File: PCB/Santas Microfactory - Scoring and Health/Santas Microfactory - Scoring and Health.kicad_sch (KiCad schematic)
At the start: 0 parts

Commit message: Scoring and Health Board Layout Done
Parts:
- added D1, D10, D100, D101, D102, D103, D104, D105, D106, D107, D108, D109, D11, D110, D111, D112, D113, D114, D115, D116, D117, D118, D119, D12, D120, D121, D122, D123, D124, D125, D126, D127, D128, D129, D13, D130, D131, D132, D133, D134, D135, D136, D137, D138, D139, D14, D140, D141, D142, D143, D144, D145, D146, D147, D148, D149, D15, D150, D151, D152, D153, D154, D155, D156, D157, D158, D159, D16, D160, D161, D162, D163, D164, D165, D166, D167, D168, D169, D17, D170, D171, D172, D173, D174, D175, D176, D177, D178, D179, D18, D180, D181, D182, D183, D184, D185, D186, D187, D188, D189, D19, D190, D191, D192, D193, D194, D195, D196, D197, D198, D199, D2, D20, D200, D201, D202, D203, D204, D205, D206, D207, D208, D209, D21, D210, D211, D212, D213, D214, D215, D216, D217, D218, D219, D22, D220, D221, D222, D223, D224, D225, D226, D227, D228, D229, D23, D230, D231, D232, D233, D234, D235, D236, D237, D238, D239, D24, D240, D241, D242, D243, D244, D245, D246, D247, D248, D249, D25, D250, D251, D252, D253, D254, D255, D256, D257, D258, D259, D26, D260, D261, D262, D263, D264, D265, D266, D267, D268, D269, D27, D270, D271, D272, D273, D274, D275, D276, D277, D278, D279, D28, D280, D281, D282, D283, D284, D285, D286, D287, D288, D289, D29, D290, D291, D292, D293, D294, D295, D296, D297, D298, D299, D3, D30, D300, D301, D302, D303, D304, D305, D306, D307, D308, D309, D31, D310, D311, D312, D313, D32, D33, D34, D35, D36, D37, D38, D39, D4, D40, D41, D42, D43, D44, D45, D46, D47, D48, D49, D5, D50, D51, D52, D53, D54, D55, D56, D57, D58, D59, D6, D60, D61, D62, D63, D64, D65, D66, D67, D68, D69, D7, D70, D71, D72, D73, D74, D75, D76, D77, D78, D79, D8, D80, D81, D82, D83, D84, D85, D86, D87, D88, D89, D9, D90, D91, D92, D93, D94, D95, D96, D97, D98, D99: D, Diode_THT:D_DO-35_SOD27_P2.54mm_Vertical_AnodeUp, symbol Device:D
- added J2: Conn_01x08_Pin, Connector_PinHeader_2.54mm:PinHeader_1x08_P2.54mm_Horizontal, symbol Connector:Conn_01x08_Pin
- added J3: Conn_01x04_Pin, Connector_PinHeader_2.54mm:PinHeader_1x04_P2.54mm_Horizontal, symbol Connector:Conn_01x04_Pin
- added J4: Bus_PCI_Express_x16, Connector_PCBEdge:BUS_PCIexpress_x16, symbol Connector:Bus_PCI_Express_x16
- added Q1, Q10, Q11, Q12, Q13, Q14, Q15, Q16, Q17, Q18, Q19, Q2, Q20, Q21, Q22, Q23, Q24, Q25, Q26, Q27, Q28, Q29, Q3, Q30, Q31, Q32, Q33, Q34, Q35, Q36, Q37, Q38, Q39, Q4, Q40, Q41, Q42, Q43, Q44, Q45, Q46, Q47, Q48, Q49, Q5, Q50, Q51, Q52, Q53, Q54, Q55, Q56, Q57, Q58, Q59, Q6, Q60, Q61, Q62, Q63, Q64, Q65, Q66, Q67, Q68, Q69, Q7, Q70, Q71, Q72, Q73, Q74, Q75, Q76, Q77, Q78, Q79, Q8, Q80, Q81, Q9: NPN, Package_TO_SOT_THT:TO-92L_Inline, symbol Simulation_SPICE:NPN
- added R1, R10, R100, R101, R102, R103, R104, R105, R106, R107, R108, R109, R11, R110, R111, R112, R113, R114, R115, R116, R117, R118, R119, R12, R120, R121, R122, R123, R124, R125, R126, R127, R128, R129, R13, R130, R131, R132, R133, R134, R135, R136, R137, R138, R139, R14, R140, R141, R142, R143, R144, R145, R146, R147, R148, R149, R15, R150, R151, R152, R153, R154, R155, R156, R157, R158, R159, R16, R160, R161, R162, R163, R164, R165, R166, R167, R168, R169, R17, R170, R171, R172, R173, R174, R175, R176, R177, R178, R179, R18, R180, R181, R182, R183, R184, R185, R186, R187, R188, R189, R19, R190, R191, R192, R193, R194, R195, R196, R197, R198, R199, R2, R20, R200, R201, R202, R203, R204, R205, R206, R207, R208, R209, R21, R210, R211, R212, R213, R214, R215, R216, R217, R218, R219, R22, R220, R221, R222, R223, R224, R225, R226, R227, R228, R229, R23, R230, R231, R232, R233, R24, R25, R26, R27, R28, R29, R3, R30, R31, R32, R33, R34, R35, R36, R37, R38, R39, R4, R40, R41, R42, R43, R44, R45, R46, R47, R48, R49, R5, R50, R51, R52, R53, R54, R55, R56, R57, R58, R59, R6, R60, R61, R62, R63, R64, R65, R66, R67, R68, R69, R7, R70, R71, R72, R73, R74, R75, R76, R77, R78, R79, R8, R80, R81, R82, R83, R84, R85, R86, R87, R88, R89, R9, R90, R91, R92, R93, R94, R95, R96, R97, R98, R99: 10k, Resistor_THT:R_Axial_DIN0207_L6.3mm_D2.5mm_P2.54mm_Vertical, symbol Device:R
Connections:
- new net: D13.2 (A), D14.1 (K), D30.2 (A), R20.2
- new net: D14.2 (A), D31.2 (A), Q2.2 (B), R21.2
- new net: D155.1 (K), Q46.1 (C), R150.2
- new net: D155.2 (A), D180.2 (A), D207.2 (A), R118.2
- new net: D110.2 (A), D94.2 (A), Q24.2 (B), R81.2
- new net: D4.2 (A), D50.1 (K), D9.2 (A), Q11.2 (B), R8.2
- new net: D19.2 (A), D20.1 (K), D36.2 (A), R26.2
- new net: D20.2 (A), D37.2 (A), Q5.2 (B), R27.2
- new net: D122.2 (A), D138.2 (A), D146.1 (K), R101.2
- new net: D274.1 (K), Q75.1 (C), R226.2
- new net: D231.2 (A), D232.1 (K), D244.2 (A), R184.2
- new net: D276.2 (A), D286.2 (A), D287.2 (A), R207.2
- new net: D33.1 (K), D49.1 (K), Q15.1 (C), R36.2
- new net: D56.2 (A), D73.2 (A), Q15.2 (B), R52.2
- new net: D19.1 (K), Q11.1 (C), R16.2
- new net: D47.2 (A), D64.2 (A), D72.1 (K), R43.2
- new net: D158.2 (A), D184.2 (A), D185.2 (A), R121.2
- new net: D100.1 (K), D115.2 (A), D99.2 (A), R86.2
- new net: D17.2 (A), D18.1 (K), D34.2 (A), R24.2
- new net: D18.2 (A), D35.2 (A), Q4.2 (B), R25.2
- new net: D294.2 (A), D303.2 (A), Q72.2 (B), R218.2
- new net: D248.2 (A), D261.2 (A), D267.1 (K), R192.2
- new net: D254.2 (A), D267.2 (A), Q66.2 (B), R198.2
- new net: D108.1 (K), D122.1 (K), Q35.1 (C), R92.2
- new net: D252.2 (A), D265.2 (A), D271.1 (K), R196.2
- new net: D258.2 (A), D271.2 (A), Q70.2 (B), R202.2
- new net: D153.2 (A), D177.2 (A), D206.2 (A), R116.2
- new net: D259.2 (A), D272.2 (A), Q71.2 (B), R203.2
- new net: D51.2 (A), D68.2 (A), D76.1 (K), R47.2
- new net: D235.1 (K), D249.1 (K), Q66.1 (C), R186.2
- new net: D11.1 (K), Q9.1 (C), R14.2
- new net: D11.2 (A), D12.1 (K), D28.2 (A), R18.2
- new net: D17.1 (K), D56.1 (K), Q3.1 (C), R6.2
- new net: D16.2 (A), D33.2 (A), Q3.2 (B), R23.2
- new net: D15.2 (A), D16.1 (K), D32.2 (A), R22.2
- new net: D161.1 (K), Q52.1 (C), R156.2
- new net: D161.2 (A), D189.2 (A), D210.2 (A), R124.2
- new net: D107.2 (A), D91.2 (A), D92.1 (K), R78.2
- new net: D163.2 (A), D192.2 (A), D211.2 (A), R126.2
- new net: D251.2 (A), D264.2 (A), D270.1 (K), R195.2
- new net: D131.1 (K), D97.1 (K), Q25.1 (C), R65.2
- new net: D119.1 (K), D79.2 (A), D83.2 (A), Q29.2 (B), R58.2
- new net: D87.1 (K), Q29.1 (C), R70.2
- new net: D116.1 (K), D126.1 (K), Q39.1 (C), R96.2
- new net: D55.2 (A), D72.2 (A), Q14.2 (B), R51.2
- new net: D250.2 (A), D263.2 (A), D269.1 (K), R194.2
- new net: D157.1 (K), Q48.1 (C), R152.2
- new net: D123.2 (A), D139.2 (A), D147.1 (K), R102.2
- new net: D131.2 (A), D147.2 (A), Q37.2 (B), R110.2
- new net: D41.1 (K), D53.1 (K), Q19.1 (C), R40.2
- new net: D24.2 (A), D41.2 (A), Q7.2 (B), R31.2
- new net: D273.2 (A), D282.2 (A), D299.2 (A), R204.2
- new net: D121.1 (K), D80.2 (A), D84.2 (A), Q30.2 (B), R61.2
- new net: D13.1 (K), D54.1 (K), Q1.1 (C), R3.2
- new net: D12.2 (A), D29.2 (A), Q1.2 (B), R19.2
- new net: D22.2 (A), D39.2 (A), Q6.2 (B), R29.2
- new net: D91.1 (K), Q30.1 (C), R71.2
- new net: D130.2 (A), D146.2 (A), Q36.2 (B), R109.2
- new net: D109.2 (A), D93.2 (A), D94.1 (K), R80.2
- new net: D158.1 (K), Q47.1 (C), R151.2
- new net: D120.2 (A), D136.2 (A), D144.1 (K), R99.2
- new net: D123.1 (K), D81.2 (A), D85.2 (A), Q31.2 (B), R64.2
- new net: D133.2 (A), D149.2 (A), Q39.2 (B), R112.2
- new net: D224.2 (A), D237.2 (A), Q58.2 (B), R177.2
- new net: D119.2 (A), D135.2 (A), D143.1 (K), R98.2
- new net: D215.2 (A), D219.2 (A), D250.1 (K), Q64.2 (B), R165.2
- new net: D273.1 (K), Q76.1 (C), R227.2
- new net: D112.1 (K), D124.1 (K), Q37.1 (C), R94.2
- new net: D112.2 (A), D96.2 (A), Q25.2 (B), R83.2
- new net: D23.1 (K), Q12.1 (C), R17.2
- new net: D46.2 (A), D63.2 (A), D71.1 (K), R42.2
- new net: D151.1 (K), Q42.1 (C), R146.2
- new net: D154.2 (A), D178.2 (A), D179.2 (A), R117.2
- new net: D166.1 (K), Q55.1 (C), R159.2
- new net: D152.1 (K), Q41.1 (C), R145.2
- new net: D214.2 (A), D218.2 (A), D248.1 (K), Q63.2 (B), R162.2
- new net: D125.1 (K), D82.2 (A), D86.2 (A), Q32.2 (B), R67.2
- new net: D229.1 (K), Q65.1 (C), R173.2
- new net: D216.2 (A), D220.2 (A), D252.1 (K), Q65.2 (B), R168.2
- new net: D154.1 (K), Q43.1 (C), R147.2
- new net: D275.1 (K), Q78.1 (C), R229.2
- new net: D221.1 (K), Q63.1 (C), R171.2
- new net: D100.2 (A), D116.2 (A), Q27.2 (B), R87.2
- new net: D160.2 (A), D187.2 (A), D188.2 (A), R123.2
- new net: D53.2 (A), D70.2 (A), D78.1 (K), R49.2
- new net: D152.2 (A), D175.2 (A), D176.2 (A), R115.2
- new net: D278.1 (K), Q79.1 (C), R230.2
- new net: D10.2 (A), D5.2 (A), D52.1 (K), Q12.2 (B), R11.2
- new net: D23.2 (A), D24.1 (K), D40.2 (A), R30.2
- new net: D127.1 (K), D89.1 (K), Q21.1 (C), R59.2
- new net: D25.2 (A), D26.1 (K), D42.2 (A), R32.2
- new net: D101.1 (K), D133.1 (K), Q27.1 (C), R68.2
- new net: D101.2 (A), D102.1 (K), D117.2 (A), R88.2
- new net: D153.1 (K), Q44.1 (C), R148.2
- new net: D61.2 (A), D78.2 (A), Q20.2 (B), R57.2
- new net: D164.2 (A), D193.2 (A), D194.2 (A), R127.2
- new net: D312.2 (A), D313.2 (A), Q81.2 (B), R233.2
- new net: D121.2 (A), D137.2 (A), D145.1 (K), R100.2
- new net: D157.2 (A), D183.2 (A), D208.2 (A), R120.2
- new net: D151.2 (A), D174.2 (A), D205.2 (A), R114.2
- new net: D274.2 (A), D283.2 (A), D284.2 (A), R205.2
- new net: D166.2 (A), D196.2 (A), D197.2 (A), R129.2
- new net: D165.2 (A), D195.2 (A), D212.2 (A), R128.2
- new net: D253.2 (A), D266.2 (A), D272.1 (K), R197.2
- new net: D50.2 (A), D67.2 (A), D75.1 (K), R46.2
- new net: D37.1 (K), D51.1 (K), Q17.1 (C), R38.2
- new net: D113.2 (A), D97.2 (A), D98.1 (K), R84.2
- new net: D25.1 (K), D60.1 (K), Q7.1 (C), R12.2
- new net: D15.1 (K), Q10.1 (C), R15.2
- new net: D223.1 (K), D254.1 (K), Q57.1 (C), R163.2
- new net: D222.2 (A), D235.2 (A), Q57.2 (B), R175.2
- new net: D125.2 (A), D141.2 (A), D149.1 (K), R104.2
- new net: D2.2 (A), D46.1 (K), D7.2 (A), Q9.2 (B), R2.2
- new net: D243.1 (K), D253.1 (K), Q70.1 (C), R190.2
- new net: D127.2 (A), D143.2 (A), Q33.2 (B), R106.2
- new net: D29.1 (K), D47.1 (K), Q13.1 (C), R34.2
- new net: D54.2 (A), D71.2 (A), Q13.2 (B), R50.2
- new net: D26.2 (A), D43.2 (A), Q8.2 (B), R33.2
- new net: D304.1 (K), Q74.1 (C), R219.2
- new net: D232.2 (A), D245.2 (A), Q62.2 (B), R185.2
- new net: D278.2 (A), D289.2 (A), D290.2 (A), R209.2
- new net: D225.2 (A), D226.1 (K), D238.2 (A), R178.2
- new net: D226.2 (A), D239.2 (A), Q59.2 (B), R179.2
- new net: D57.2 (A), D74.2 (A), Q16.2 (B), R53.2
- new net: D111.2 (A), D95.2 (A), D96.1 (K), R82.2
- new net: D49.2 (A), D66.2 (A), D74.1 (K), R45.2
- new net: D229.2 (A), D230.1 (K), D242.2 (A), R182.2
- new net: D48.2 (A), D65.2 (A), D73.1 (K), R44.2
- new net: D102.2 (A), D118.2 (A), Q28.2 (B), R89.2
- new net: D221.2 (A), D222.1 (K), D234.2 (A), R174.2
- new net: D164.1 (K), Q53.1 (C), R157.2
- new net: D126.2 (A), D142.2 (A), D150.1 (K), R105.2
- new net: D134.2 (A), D150.2 (A), Q40.2 (B), R113.2
- new net: D162.2 (A), D190.2 (A), D191.2 (A), R125.2
- new net: D160.1 (K), Q49.1 (C), R153.2
- new net: D277.1 (K), Q80.1 (C), R231.2
- new net: D162.1 (K), Q51.1 (C), R155.2
- new net: D281.2 (A), D293.2 (A), D307.1 (K), R214.2
- new net: D277.2 (A), D288.2 (A), D301.2 (A), R208.2
- new net: D257.2 (A), D270.2 (A), Q69.2 (B), R201.2
- new net: D227.2 (A), D228.1 (K), D240.2 (A), R180.2
- new net: D114.2 (A), D98.2 (A), Q26.2 (B), R85.2
- new net: D59.2 (A), D76.2 (A), Q18.2 (B), R55.2
- new net: D163.1 (K), Q54.1 (C), R158.2
- new net: D106.2 (A), D90.2 (A), Q22.2 (B), R77.2
- new net: D129.1 (K), D93.1 (K), Q23.1 (C), R62.2
- new net: D228.2 (A), D241.2 (A), Q60.2 (B), R181.2
- new net: D276.1 (K), Q77.1 (C), R228.2
- new net: D256.2 (A), D269.2 (A), Q68.2 (B), R200.2
- new net: D129.2 (A), D145.2 (A), Q35.2 (B), R108.2
- new net: D132.2 (A), D148.2 (A), Q38.2 (B), R111.2
- new net: D159.1 (K), Q50.1 (C), R154.2
- new net: D227.1 (K), D256.1 (K), Q59.1 (C), R166.2
- new net: D124.2 (A), D140.2 (A), D148.1 (K), R103.2
- new net: D223.2 (A), D224.1 (K), D236.2 (A), R176.2
- new net: D103.2 (A), D87.2 (A), D88.1 (K), R74.2
- new net: D255.2 (A), D268.2 (A), Q67.2 (B), R199.2
- new net: D298.1 (K), D308.1 (K), Q73.2 (B), R223.1
- new net: D104.1 (K), D120.1 (K), Q33.1 (C), R90.2
- new net: D3.2 (A), D48.1 (K), D8.2 (A), Q10.2 (B), R5.2
- new net: D156.2 (A), D181.2 (A), D182.2 (A), R119.2
- new net: D99.1 (K), Q32.1 (C), R73.2
- new net: D105.2 (A), D89.2 (A), D90.1 (K), R76.2
- new net: D156.1 (K), Q45.1 (C), R149.2
- new net: D58.2 (A), D75.2 (A), Q17.2 (B), R54.2
- new net: D231.1 (K), D258.1 (K), Q61.1 (C), R169.2
- new net: D21.1 (K), D58.1 (K), Q5.1 (C), R9.2
- new net: D230.2 (A), D243.2 (A), Q61.2 (B), R183.2
- new net: D302.2 (A), D309.2 (A), Q74.2 (B), R224.2
- new net: D159.2 (A), D186.2 (A), D209.2 (A), R122.2
- new net: D225.1 (K), Q64.1 (C), R172.2
- new net: D60.2 (A), D77.2 (A), Q19.2 (B), R56.2
- new net: D275.2 (A), D285.2 (A), D300.2 (A), R206.2
- new net: D52.2 (A), D69.2 (A), D77.1 (K), R48.2
- new net: D95.1 (K), Q31.1 (C), R72.2
- new net: D128.2 (A), D144.2 (A), Q34.2 (B), R107.2
- new net: D108.2 (A), D92.2 (A), Q23.2 (B), R79.2
- new net: D21.2 (A), D22.1 (K), D38.2 (A), R28.2
- new net: D249.2 (A), D262.2 (A), D268.1 (K), R193.2
- new net: D165.1 (K), Q56.1 (C), R160.2
- new net: D239.1 (K), D251.1 (K), Q68.1 (C), R188.2
- new net: D293.1 (K), Q73.1 (C), R213.2
- new net: D104.2 (A), D88.2 (A), Q21.2 (B), R75.2
- new net +5V: J4.A10 (+3.3V), J4.A2 (+12V), J4.A3 (+12V), J4.A9 (+3.3V), J4.B1 (+12V), J4.B10 (3.3Vaux), J4.B2 (+12V), J4.B3 (+12V), J4.B8 (+3.3V), R10.1, R100.1, R101.1, R102.1, R103.1, R104.1, R105.1, R106.1, R107.1, R108.1, R109.1, R11.1, R110.1, R111.1, R112.1, R113.1, R114.1, R115.1, R116.1, R117.1, R118.1, R119.1, R12.1, R120.1, R121.1, R122.1, R123.1, R124.1, R125.1, R126.1, R127.1, R128.1, R129.1, R13.1, R130.1, R131.1, R132.1, R133.1, R134.1, R135.1, R136.1, R14.1, R145.1, R146.1, R147.1, R148.1, R149.1, R15.1, R150.1, R151.1, R152.1, R153.1, R154.1, R155.1, R156.1, R157.1, R158.1, R159.1, R16.1, R160.1, R162.1, R163.1, R164.1, R165.1, R166.1, R167.1, R168.1, R169.1, R17.1, R170.1, R171.1, R172.1, R173.1, R174.1, R175.1, R176.1, R177.1, R178.1, R179.1, R18.1, R180.1, R181.1, R182.1, R183.1, R184.1, R185.1, R186.1, R187.1, R188.1, R189.1, R19.1, R190.1, R191.1, R192.1, R193.1, R194.1, R195.1, R196.1, R197.1, R198.1, R199.1, R2.1, R20.1, R200.1, R201.1, R202.1, R203.1, R204.1, R205.1, R206.1, R207.1, R208.1, R209.1, R21.1, R210.1, R211.1, R212.1, R213.1, R214.1, R218.1, R219.1, R22.1, R220.1, R221.1, R222.1, R224.1, R225.1, R226.1, R227.1, R228.1, R229.1, R23.1, R230.1, R231.1, R232.1, R233.1, R24.1, R25.1, R26.1, R27.1, R28.1, R29.1, R3.1, R30.1, R31.1, R32.1, R33.1, R34.1, R35.1, R36.1, R37.1, R38.1, R39.1, R4.1, R40.1, R41.1, R42.1, R43.1, R44.1, R45.1, R46.1, R47.1, R48.1, R49.1, R5.1, R50.1, R51.1, R52.1, R53.1, R54.1, R55.1, R56.1, R57.1, R58.1, R59.1, R6.1, R60.1, R61.1, R62.1, R63.1, R64.1, R65.1, R66.1, R67.1, R68.1, R69.1, R7.1, R70.1, R71.1, R72.1, R73.1, R74.1, R75.1, R76.1, R77.1, R78.1, R79.1, R8.1, R80.1, R81.1, R82.1, R83.1, R84.1, R85.1, R86.1, R87.1, R88.1, R89.1, R9.1, R90.1, R91.1, R92.1, R93.1, R94.1, R95.1, R96.1, R97.1, R98.1, R99.1
- new net CLK: D103.1 (K), D107.1 (K), D111.1 (K), D115.1 (K), D135.1 (K), D137.1 (K), D139.1 (K), D141.1 (K), D234.1 (K), D238.1 (K), D242.1 (K), D261.1 (K), D263.1 (K), D265.1 (K), D28.1 (K), D32.1 (K), D36.1 (K), D40.1 (K), D63.1 (K), D65.1 (K), D67.1 (K), D69.1 (K), J4.A13 (REFCLK+)
- new net CLK_TICK: J4.A1 (~{PRSNT1})
- new net CORR_0: D1.2 (A), J4.B82 (RSVD)
- new net CORR_1: D6.2 (A), J4.A50 (RSVD)
- new net CORR_2: D27.2 (A), J4.A33 (RSVD)
- new net CORR_3: D44.2 (A), J4.B30 (RSVD)
- new net CORR_4: D45.2 (A), J4.A32 (RSVD)
- new net CORR_5: D62.2 (A), J4.A19 (RSVD)
- new net DAMAGE: D213.1 (K), D217.1 (K), D233.1 (K), D246.1 (K), D247.1 (K), D260.1 (K), D279.1 (K), D282.1 (K), Q75.2 (B), R161.1
- new net DEATH: D294.1 (K), D307.2 (A), D311.2 (A), R225.2
- new net DSTEP1: D279.2 (A), D280.1 (K), D285.1 (K), D291.2 (A), Q77.2 (B), R211.2
- new net DSTEP2: D280.2 (A), D288.1 (K), D292.2 (A), Q79.2 (B), R212.2
- new net GND: J4.A12 (GND), J4.A15 (GND), J4.A18 (GND), J4.A20 (GND), J4.A23 (GND), J4.A24 (GND), J4.A27 (GND), J4.A28 (GND), J4.A31 (GND), J4.A34 (GND), J4.A37 (GND), J4.A38 (GND), J4.A4 (GND), J4.A41 (GND), J4.A42 (GND), J4.A45 (GND), J4.A46 (GND), J4.A49 (GND), J4.A51 (GND), J4.A54 (GND), J4.A55 (GND), J4.A58 (GND), J4.A59 (GND), J4.A62 (GND), J4.A63 (GND), J4.A66 (GND), J4.A67 (GND), J4.A70 (GND), J4.A71 (GND), J4.A74 (GND), J4.A75 (GND), J4.A78 (GND), J4.A79 (GND), J4.A82 (GND), J4.B13 (GND), J4.B16 (GND), J4.B18 (GND), J4.B21 (GND), J4.B22 (GND), J4.B25 (GND), J4.B26 (GND), J4.B29 (GND), J4.B32 (GND), J4.B35 (GND), J4.B36 (GND), J4.B39 (GND), J4.B4 (GND), J4.B40 (GND), J4.B43 (GND), J4.B44 (GND), J4.B47 (GND), J4.B49 (GND), J4.B52 (GND), J4.B53 (GND), J4.B56 (GND), J4.B57 (GND), J4.B60 (GND), J4.B61 (GND), J4.B64 (GND), J4.B65 (GND), J4.B68 (GND), J4.B69 (GND), J4.B7 (GND), J4.B72 (GND), J4.B73 (GND), J4.B76 (GND), J4.B77 (GND), J4.B80 (GND), Q1.3 (E), Q10.3 (E), Q11.3 (E), Q12.3 (E), Q13.3 (E), Q14.3 (E), Q15.3 (E), Q16.3 (E), Q17.3 (E), Q18.3 (E), Q19.3 (E), Q2.3 (E), Q20.3 (E), Q21.3 (E), Q22.3 (E), Q23.3 (E), Q24.3 (E), Q25.3 (E), Q26.3 (E), Q27.3 (E), Q28.3 (E), Q29.3 (E), Q3.3 (E), Q30.3 (E), Q31.3 (E), Q32.3 (E), Q33.3 (E), Q34.3 (E), Q35.3 (E), Q36.3 (E), Q37.3 (E), Q38.3 (E), Q39.3 (E), Q4.3 (E), Q40.3 (E), Q41.3 (E), Q42.3 (E), Q43.3 (E), Q44.3 (E), Q45.3 (E), Q46.3 (E), Q47.3 (E), Q48.3 (E), Q49.3 (E), Q5.3 (E), Q50.3 (E), Q51.3 (E), Q52.3 (E), Q53.3 (E), Q54.3 (E), Q55.3 (E), Q56.3 (E), Q57.3 (E), Q58.3 (E), Q59.3 (E), Q6.3 (E), Q60.3 (E), Q61.3 (E), Q62.3 (E), Q63.3 (E), Q64.3 (E), Q65.3 (E), Q66.3 (E), Q67.3 (E), Q68.3 (E), Q69.3 (E), Q7.3 (E), Q70.3 (E), Q71.3 (E), Q72.3 (E), Q73.3 (E), Q74.3 (E), Q75.3 (E), Q76.3 (E), Q77.3 (E), Q78.3 (E), Q79.3 (E), Q8.3 (E), Q80.3 (E), Q81.3 (E), Q9.3 (E), R1.2, R137.2, R138.2, R139.2, R140.2, R141.2, R142.2, R143.2, R144.2, R161.2, R215.2, R216.2, R217.2, R223.2
- new net HALT: D312.1 (K), J4.B48 (~{PRSNT2}), Q72.1 (C), R210.2
- new net HEART0: D245.1 (K), D295.1 (K), D305.1 (K), D310.1 (K), J3.1 (Pin_1), Q71.1 (C), R191.2
- new net HEART1: D295.2 (A), D304.2 (A), J3.2 (Pin_2), R220.2
- new net HEART2: D296.2 (A), D305.2 (A), J3.3 (Pin_3), R221.2
- new net HEART3: D297.2 (A), D306.2 (A), D310.2 (A), J3.4 (Pin_4), R222.2
- new net INPUT0: J4.B62 (PETp11)
- new net INPUT1: J4.B63 (PETn11)
- new net INPUT2: J4.B66 (PETp12)
- new net INPUT3: J4.B67 (PETn12)
- new net INPUT4: J4.B70 (PETp13)
- new net INPUT5: J4.B71 (PETn13)
- new net IN_C0: J4.B6 (SMDAT)
- new net IN_D0: D218.1 (K), D284.1 (K), D299.1 (K), R215.1
- new net IN_D1: D219.1 (K), D287.1 (K), D300.1 (K), R216.1
- new net IN_D2: D220.1 (K), D290.1 (K), D301.1 (K), R217.1
- new net IN_G0: J4.B5 (SMCLK)
- new net IN_H0: D176.1 (K), D205.1 (K), D7.1 (K), R137.1
- new net IN_H1: D179.1 (K), D206.1 (K), D8.1 (K), R138.1
- new net IN_H2: D182.1 (K), D207.1 (K), D9.1 (K), R139.1
- new net IN_H3: D10.1 (K), D185.1 (K), D208.1 (K), R140.1
- new net IN_H4: D188.1 (K), D209.1 (K), D83.1 (K), R141.1
- new net IN_H5: D191.1 (K), D210.1 (K), D84.1 (K), R142.1
- new net IN_H6: D194.1 (K), D211.1 (K), D85.1 (K), R143.1
- new net IN_H7: D197.1 (K), D212.1 (K), D86.1 (K), R144.1
- new net LOAD0: J4.B50 (PETp8)
- new net LOAD1: J4.B51 (PETn8)
- new net LOAD2: J4.B54 (PETp9)
- new net LOAD3: J4.B55 (PETn9)
- new net LOAD4: J4.B58 (PETp10)
- new net LOAD5: J4.B59 (PETn10)
- new net NCLK: D105.1 (K), D109.1 (K), D113.1 (K), D117.1 (K), D136.1 (K), D138.1 (K), D140.1 (K), D142.1 (K), D236.1 (K), D240.1 (K), D244.1 (K), D262.1 (K), D264.1 (K), D266.1 (K), D30.1 (K), D311.1 (K), D34.1 (K), D38.1 (K), D42.1 (K), D64.1 (K), D66.1 (K), D68.1 (K), D70.1 (K), J4.A14 (REFCLK-)
- new net NHALT: D303.1 (K), J4.B81 (~{PRSNT2}), Q81.1 (C), R232.2
- new net NOUT_D0: D237.1 (K), D297.1 (K), Q67.1 (C), R187.2
- new net NOUT_D1: D241.1 (K), D296.1 (K), D306.1 (K), Q69.1 (C), R189.2
- new net NOUT_H0: D31.1 (K), Q14.1 (C), R35.2
- new net NOUT_H1: D35.1 (K), Q16.1 (C), R37.2
- new net NOUT_H2: D39.1 (K), Q18.1 (C), R39.2
- new net NOUT_H3: D43.1 (K), Q20.1 (C), R41.2
- new net NOUT_H4: D106.1 (K), Q34.1 (C), R91.2
- new net NOUT_H5: D110.1 (K), Q36.1 (C), R93.2
- new net NOUT_H6: D114.1 (K), Q38.1 (C), R95.2
- new net NOUT_H7: D118.1 (K), Q40.1 (C), R97.2
- new net NRESET: D2.1 (K), D214.1 (K), D215.1 (K), D216.1 (K), D3.1 (K), D4.1 (K), D5.1 (K), D79.1 (K), D80.1 (K), D81.1 (K), D82.1 (K), J4.B31 (~{PRSNT2})
- new net OUT_D0: D255.1 (K), D283.1 (K), D291.1 (K), D298.2 (A), D302.1 (K), Q58.1 (C), Q76.2 (B), R164.2
- new net OUT_D1: D257.1 (K), D286.1 (K), D292.1 (K), D308.2 (A), D309.1 (K), Q60.1 (C), Q78.2 (B), R167.2
- new net OUT_D2: D259.1 (K), D281.1 (K), D289.1 (K), Q62.1 (C), Q80.2 (B), R170.2
- new net OUT_H0: D175.1 (K), D198.1 (K), D55.1 (K), J2.8 (Pin_8), Q2.1 (C), Q42.2 (B), R4.2
- new net OUT_H1: D178.1 (K), D199.1 (K), D57.1 (K), J2.7 (Pin_7), Q4.1 (C), Q44.2 (B), R7.2
- new net OUT_H2: D181.1 (K), D200.1 (K), D59.1 (K), J2.6 (Pin_6), Q46.2 (B), Q6.1 (C), R10.2
- new net OUT_H3: D184.1 (K), D201.1 (K), D61.1 (K), J2.5 (Pin_5), Q48.2 (B), Q8.1 (C), R13.2
- new net OUT_H4: D128.1 (K), D187.1 (K), D202.1 (K), J2.4 (Pin_4), Q22.1 (C), Q50.2 (B), R60.2
- new net OUT_H5: D130.1 (K), D190.1 (K), D203.1 (K), J2.3 (Pin_3), Q24.1 (C), Q52.2 (B), R63.2
- new net OUT_H6: D132.1 (K), D193.1 (K), D204.1 (K), J2.2 (Pin_2), Q26.1 (C), Q54.2 (B), R66.2
- new net OUT_H7: D134.1 (K), D196.1 (K), J2.1 (Pin_1), Q28.1 (C), Q56.2 (B), R69.2
- new net RESET: D313.1 (K), J4.B17 (~{PRSNT2})
- new net SEED_1: J4.B14 (PETp0)
- new net SEED_2: J4.B15 (PETn0)
- new net SEED_3: J4.B19 (PETp1)
- new net SEED_4: J4.B20 (PETn1)
- new net STEP0: D1.1 (K), D167.1 (K), D174.1 (K), D27.1 (K), D44.1 (K), D45.1 (K), D6.1 (K), D62.1 (K), Q41.2 (B), R1.1
- new net STEP1: D167.2 (A), D168.1 (K), D177.1 (K), D198.2 (A), Q43.2 (B), R130.2
- new net STEP2: D168.2 (A), D169.1 (K), D180.1 (K), D199.2 (A), Q45.2 (B), R131.2
- new net STEP3: D169.2 (A), D170.1 (K), D183.1 (K), D200.2 (A), Q47.2 (B), R132.2
- new net STEP4: D170.2 (A), D171.1 (K), D186.1 (K), D201.2 (A), Q49.2 (B), R133.2
- new net STEP5: D171.2 (A), D172.1 (K), D189.1 (K), D202.2 (A), Q51.2 (B), R134.2
- new net STEP6: D172.2 (A), D173.1 (K), D192.1 (K), D203.2 (A), Q53.2 (B), R135.2
- new net STEP7: D173.2 (A), D195.1 (K), D204.2 (A), Q55.2 (B), R136.2
- new net TAP_C2: J4.B24 (PETn2)
- new net TAP_C3: J4.B28 (PETn3)
- new net TAP_C5: J4.B34 (PETn4)
- new net TAP_C6: J4.B38 (PETn5)
- new net TAP_C8: J4.B42 (PETn6)
- new net TAP_C9: J4.B46 (PETn7)
- new net TAP_G2: J4.B23 (PETp2)
- new net TAP_G3: J4.B27 (PETp3)
- new net TAP_G5: J4.B33 (PETp4)
- new net TAP_G6: J4.B37 (PETp5)
- new net TAP_G8: J4.B41 (PETp6)
- new net TAP_G9: J4.B45 (PETp7)
- new net WRONG_0: D213.2 (A), J4.B12 (RSVD)
- new net WRONG_1: D217.2 (A), J4.B11 (~{WAKE})
- new net WRONG_2: D233.2 (A), J4.A11 (~{PERST})
- new net WRONG_3: D246.2 (A), J4.B9 (JTAG1)
- new net WRONG_4: D247.2 (A), J4.A5 (JTAG2)
- new net WRONG_5: D260.2 (A), J4.A6 (JTAG3)
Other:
- note added: "AND"
- note added: "D Flip-Flop"
- note added: "NAND"
- note added: "NOT"
- note added: "OR"
- note added: "RESETMASK"
- note added: "SCORE / HEALTH"
- note added: "SR Latch"
- note added: "XOR"

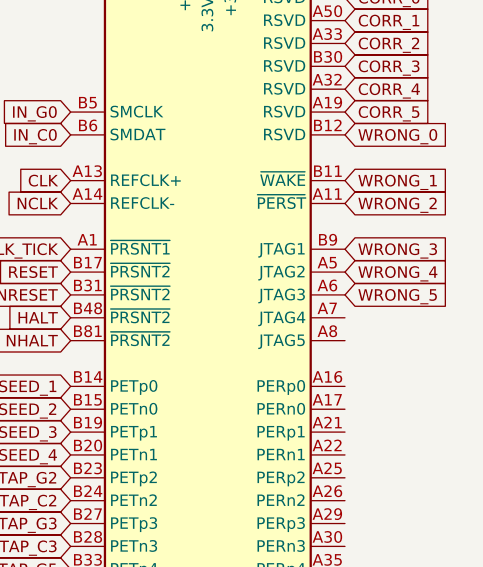
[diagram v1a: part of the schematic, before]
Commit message: Finished Backplane
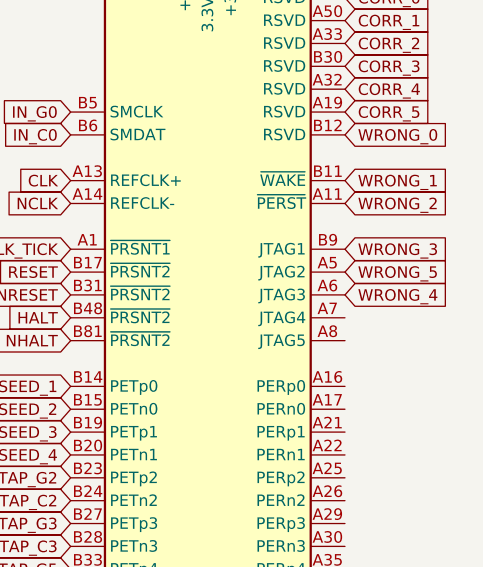
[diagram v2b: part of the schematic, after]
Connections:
- net WRONG_4: now also J4.A6 (JTAG3); no longer J4.A5 (JTAG2)
- net WRONG_5: now also J4.A5 (JTAG2); no longer J4.A6 (JTAG3)
